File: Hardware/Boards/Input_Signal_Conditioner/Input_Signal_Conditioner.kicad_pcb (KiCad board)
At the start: 2 copper layers, 20 parts, among them J1 Conn_01x01, J2 Conn_01x01, J3 Conn_01x05, J4 Conn_01x03, U1 LTC6256

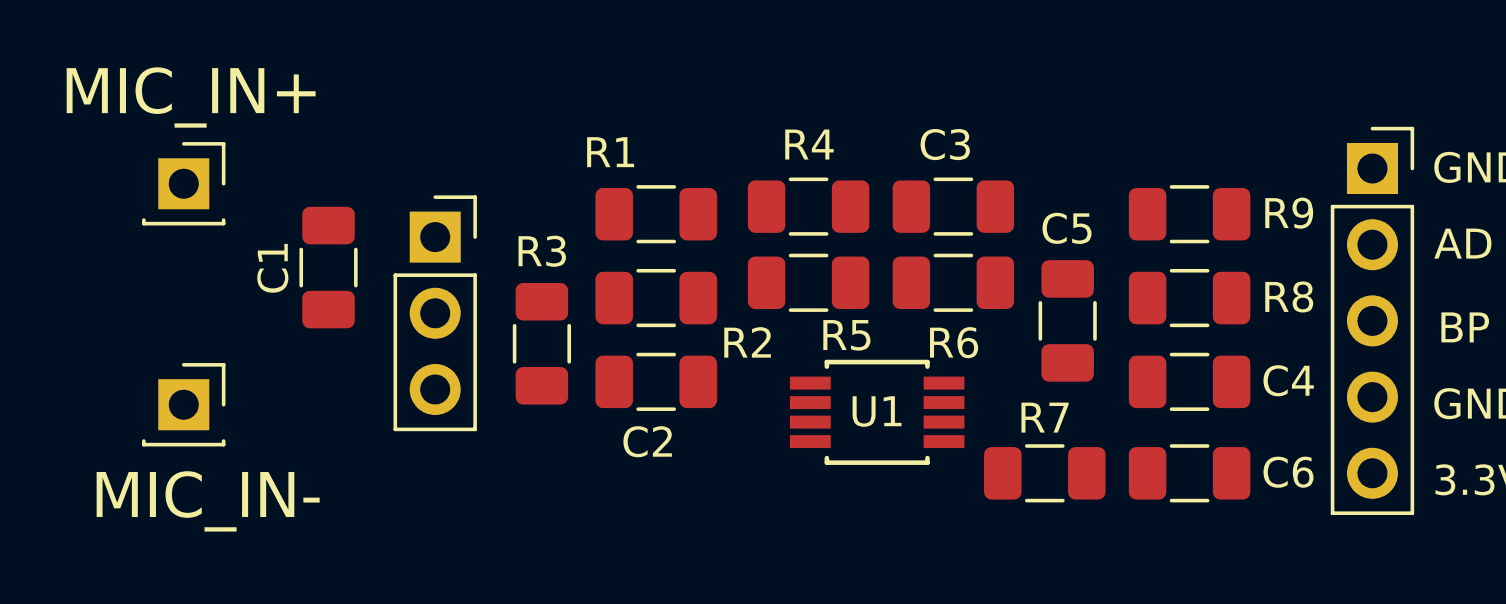
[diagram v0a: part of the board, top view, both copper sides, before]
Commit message: Redesigned the ISC LPF filter to a new cutoff frequency. Also began documentation of the ISC design. Updated the LTSpice simulation of the ISC to reflect LPF changes. Choose an Op-amp for the design.
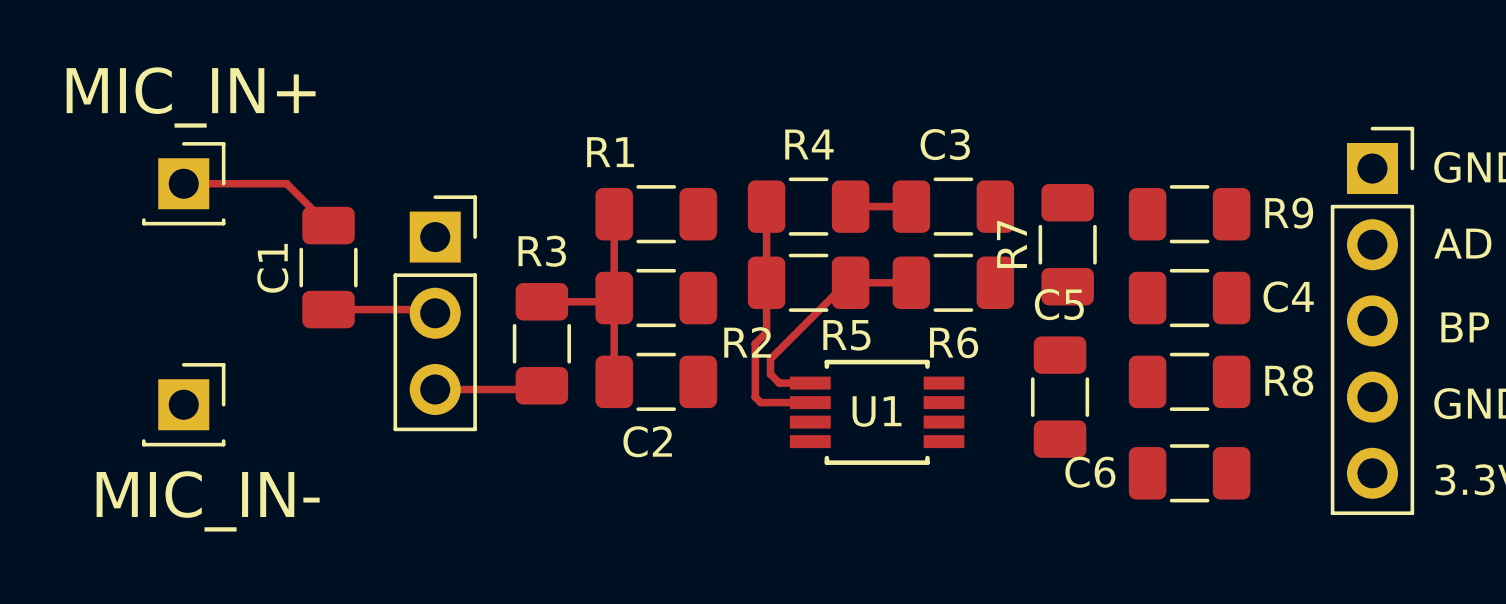
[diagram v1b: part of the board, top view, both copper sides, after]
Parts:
- U1: value LTC6256 -> LTC6256CMS8#PBF
- moved R7 7.66 mm to (143.0, 93.2), turned to 90 degrees
- moved C4 2.79 mm to (147.1, 95.0)
- moved R8 2.79 mm to (147.1, 97.8)
- moved C5 2.55 mm to (142.7, 98.3)
- turned C6 to 180 degrees
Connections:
- J3 pad 2: ADC_IN -> BYPASS
- J3 pad 3: BYPASS -> ADC_IN
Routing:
- net Net-(R4-Pad1): track 0.00 -> 8.42 mm
- net Net-(C2-Pad1): track 0.00 -> 8.05 mm
- net /FILT_IN: track 0.00 -> 7.71 mm
- net MIC_IN+: track 0.00 -> 5.40 mm
- net /AMP_IN: track 0.00 -> 3.61 mm
- net Net-(C1-Pad1): track 0.18 -> 3.61 mm
- net Net-(C3-Pad1): track 0.00 -> 2.03 mm

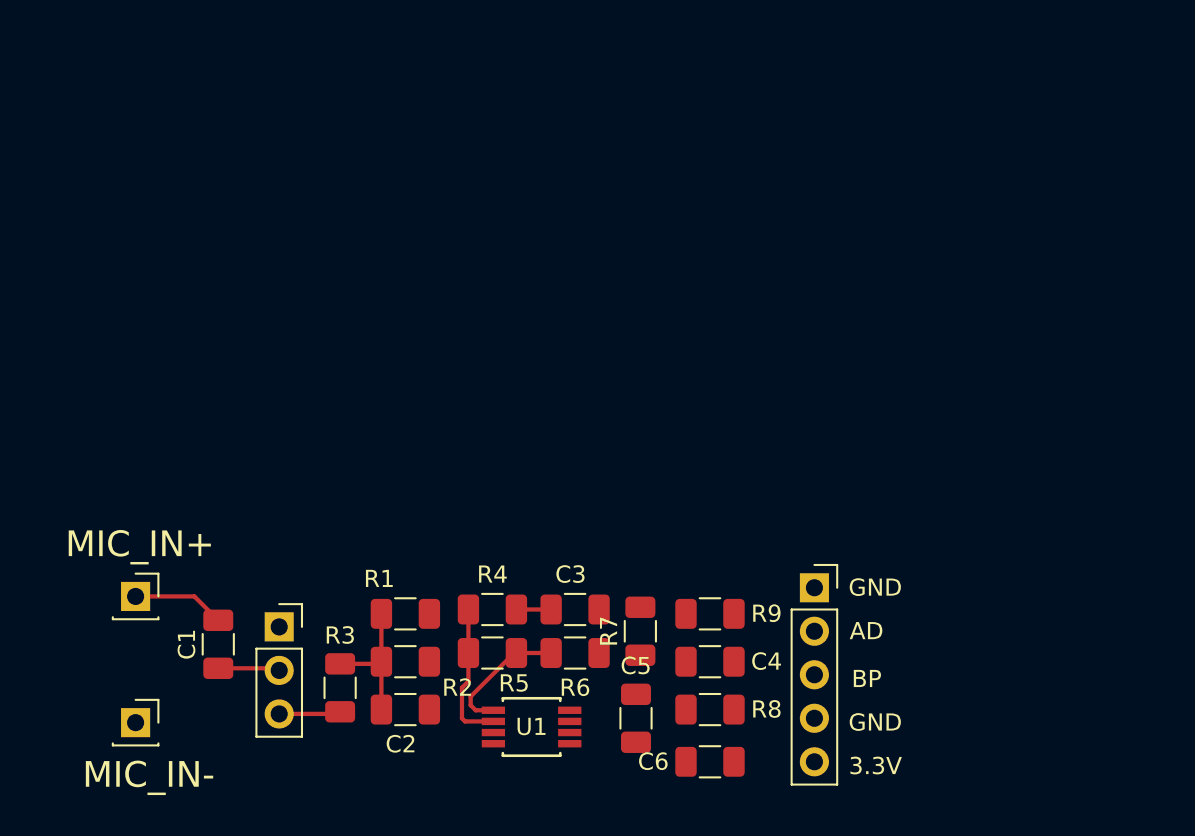
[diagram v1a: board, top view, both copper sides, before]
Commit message: Redid the layout of the PCB to be THT components. Layout needs review, then it is ready to print.
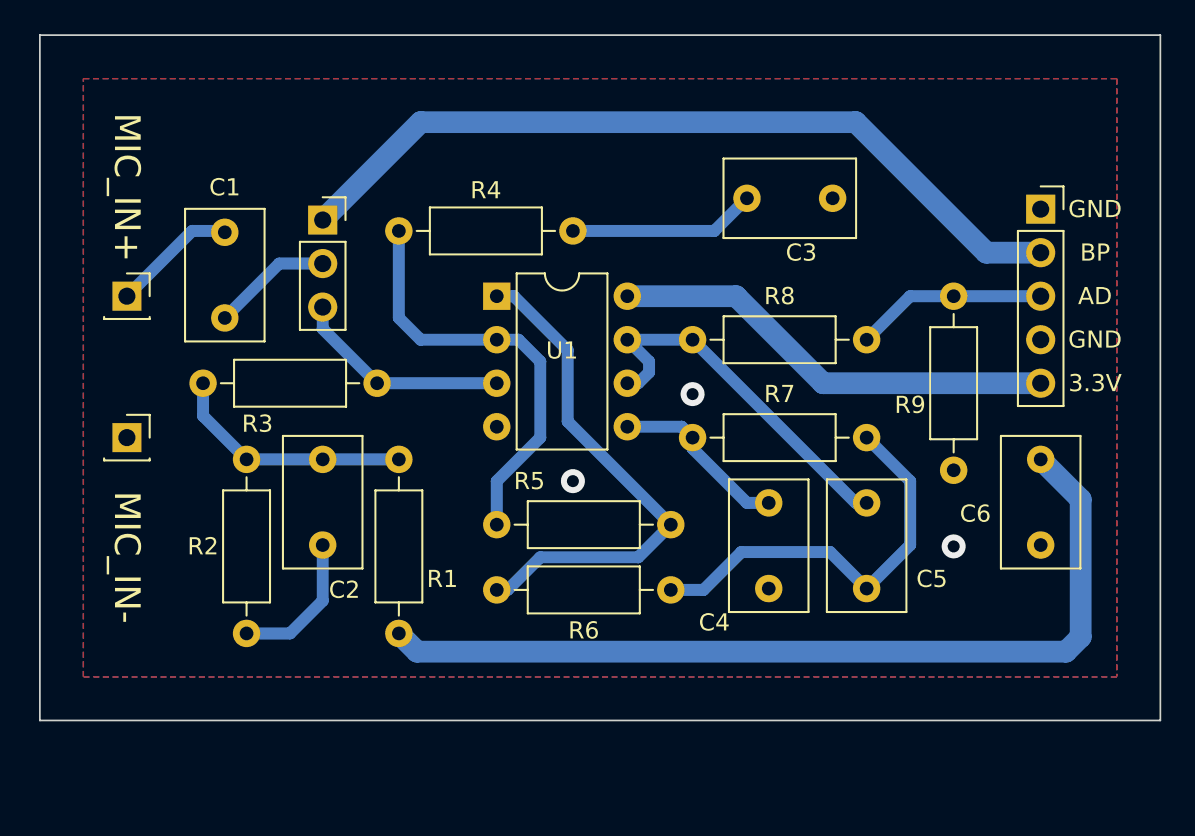
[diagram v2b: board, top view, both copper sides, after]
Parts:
- C1, C3, C6: footprint Capacitor_SMD:C_1206_3216Metric -> Capacitor_THT:C_Disc_D7.5mm_W4.4mm_P5.00mm
- C2: value 4.7u -> 4.7n; footprint Capacitor_SMD:C_1206_3216Metric -> Capacitor_THT:C_Disc_D7.5mm_W4.4mm_P5.00mm
- C4: value 2.5n -> 680p; footprint Capacitor_SMD:C_1206_3216Metric -> Capacitor_THT:C_Disc_D7.5mm_W4.4mm_P5.00mm
- C5: value 5n -> 1.5n; footprint Capacitor_SMD:C_1206_3216Metric -> Capacitor_THT:C_Disc_D7.5mm_W4.4mm_P5.00mm
- R1, R2, R3, R4, R6, R8, R9: footprint Resistor_SMD:R_1206_3216Metric -> Resistor_THT:R_Axial_DIN0207_L6.3mm_D2.5mm_P10.16mm_Horizontal
- R5: value 50K -> 11K; footprint Resistor_SMD:R_1206_3216Metric -> Resistor_THT:R_Axial_DIN0207_L6.3mm_D2.5mm_P10.16mm_Horizontal
- R7: value 11.25K -> 14.3K; footprint Resistor_SMD:R_1206_3216Metric -> Resistor_THT:R_Axial_DIN0207_L6.3mm_D2.5mm_P10.16mm_Horizontal
- U1: value LTC6256CMS8#PBF -> MCP6272; footprint LTC6256CMS8PBF:LTC6256CMS8-PBF -> Package_DIP:DIP-8_W7.62mm
- moved C6 26.2 mm to (166.4, 83.2), turned to 270 degrees
- moved C3 26.0 mm to (149.2, 67.9)
- moved J3 25.7 mm to (166.4, 68.6)
- moved U1 25.2 mm to (134.6, 73.7)
- moved J4 23.9 mm to (124.5, 69.2)
- moved R8 23.4 mm to (156.2, 76.2)
- moved R4 22.8 mm to (128.9, 69.8)
- moved C1 19.1 mm to (118.7, 74.9)
- moved C5 18.4 mm to (156.2, 85.7), turned to 270 degrees
- moved R3 17.9 mm to (127.6, 78.7), turned to 180 degrees
- moved J1 17.5 mm to (113.0, 73.7)
- moved R7 17.4 mm to (156.2, 81.9), turned to 180 degrees
- moved J2 16.6 mm to (113.0, 81.9)
- moved R9 16.5 mm to (161.3, 83.8), turned to 90 degrees
- moved C2 15.4 mm to (124.5, 83.2), turned to 270 degrees
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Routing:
- net 3.3V: track 0.00 -> 78.2 mm
- net BYPASS: track 0.00 -> 47.4 mm
- net Net-(C5-Pad2): track 0.00 -> 24.1 mm
- net /FILT_IN: track 7.71 -> 29.9 mm
- net /FILT_OUT: track 0.00 -> 21.9 mm
- net Net-(R4-Pad1): track 8.42 -> 25.0 mm
- net ADC_IN: track 0.00 -> 11.2 mm
- net Net-(C4-Pad1): track 0.00 -> 10.5 mm
- net /AMP_IN: track 3.61 -> 12.7 mm
- net Net-(C3-Pad1): track 2.03 -> 10.9 mm
- net GND: track 0.00 -> 8.49 mm, vias 0 -> 3
- net Net-(C2-Pad1): track 8.05 -> 14.4 mm
- net Net-(C1-Pad1): track 3.61 -> 7.03 mm
- net MIC_IN+: track 5.40 -> 7.33 mm
- added copper zone on B.Cu, net GND
- added copper zone on F.Cu, net GND
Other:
- board outline added: 65.4 x 40 mm

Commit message: Added mounting holes to the Input Signal Conditioner PCB. Also began citation information for ISC documentation.
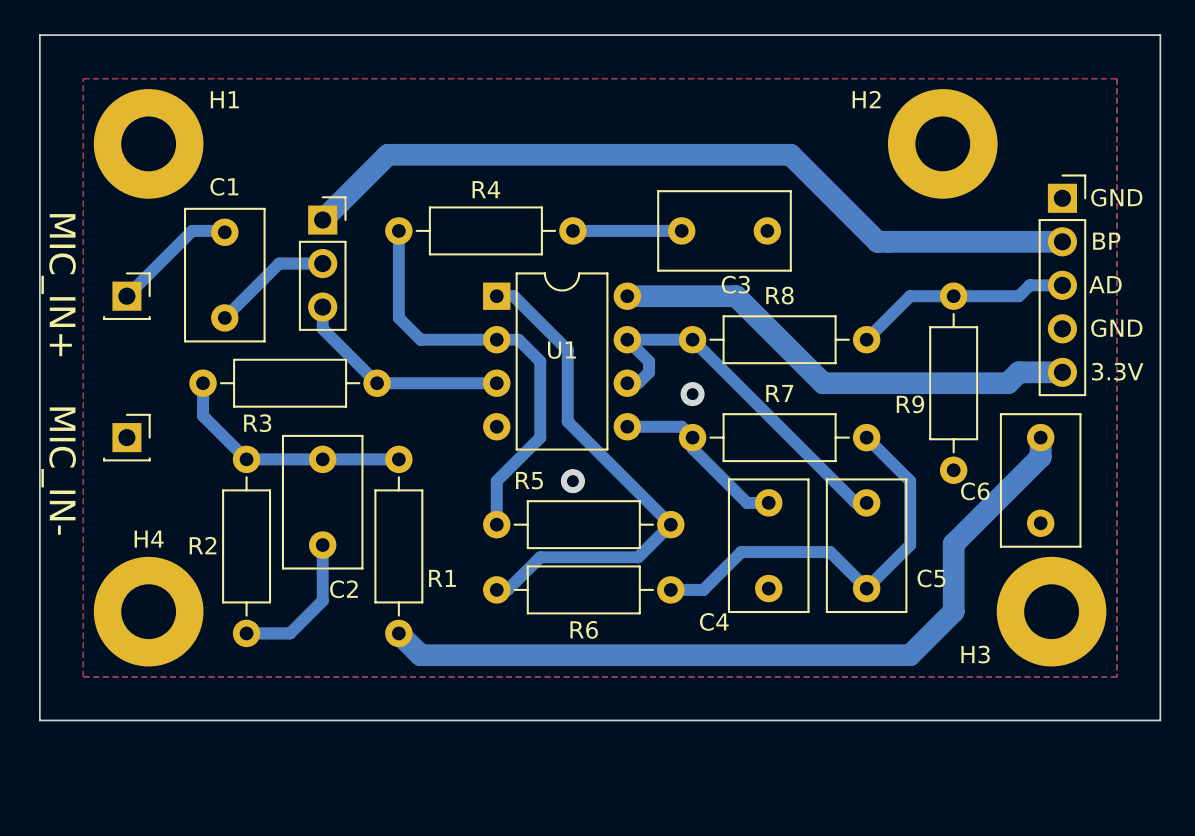
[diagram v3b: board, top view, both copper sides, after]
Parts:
- added H1: MountingHole_Pad, MountingHole:MountingHole_3.2mm_M3_Pad, F.Cu at (114.3, 64.8)
- added H2: MountingHole_Pad, MountingHole:MountingHole_3.2mm_M3_Pad, F.Cu at (160.7, 64.8)
- added H3: MountingHole_Pad, MountingHole:MountingHole_3.2mm_M3_Pad, F.Cu at (167.0, 92.1)
- added H4: MountingHole_Pad, MountingHole:MountingHole_3.2mm_M3_Pad, F.Cu at (114.3, 92.1)
- moved C3 4.26 mm to (145.4, 69.8)
- moved J3 1.42 mm to (167.6, 67.9)
- moved C6 1.27 mm to (166.4, 81.9)
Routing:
- net Net-(C3-Pad1): track 10.9 -> 6.35 mm
- net 3.3V: track 78.2 -> 74.0 mm
- net ADC_IN: track 11.2 -> 12.7 mm
- net BYPASS: track 47.4 -> 46.9 mm
- net GND: vias 3 -> 2

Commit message: Made edits suggested by Mark to the ISC pcb. Sent the board for Milling.
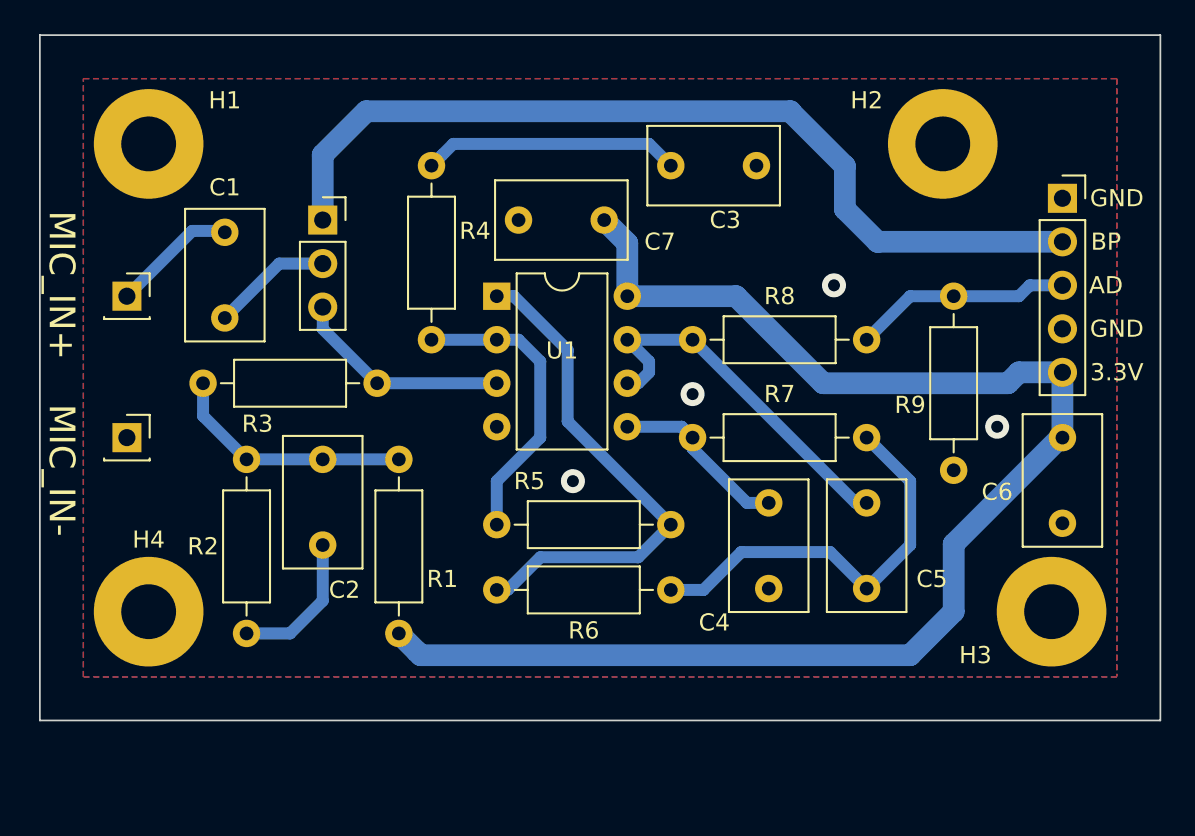
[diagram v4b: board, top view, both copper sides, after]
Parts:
- added C7: 0.1u, Capacitor_THT:C_Disc_D7.5mm_W4.4mm_P5.00mm, F.Cu at (135.9, 69.2)
- moved R4 6.63 mm to (130.8, 76.2), turned to 90 degrees
- moved C3 3.86 mm to (144.8, 66.0)
- moved C6 1.27 mm to (167.6, 81.9)
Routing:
- net 3.3V: track 74.0 -> 83.4 mm
- net Net-(C3-Pad1): track 6.35 -> 15.0 mm
- net Net-(R4-Pad1): track 25.0 -> 17.5 mm
- net BYPASS: track 46.9 -> 52.7 mm
- net GND: vias 2 -> 4
